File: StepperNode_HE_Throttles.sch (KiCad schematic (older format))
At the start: 2 parts

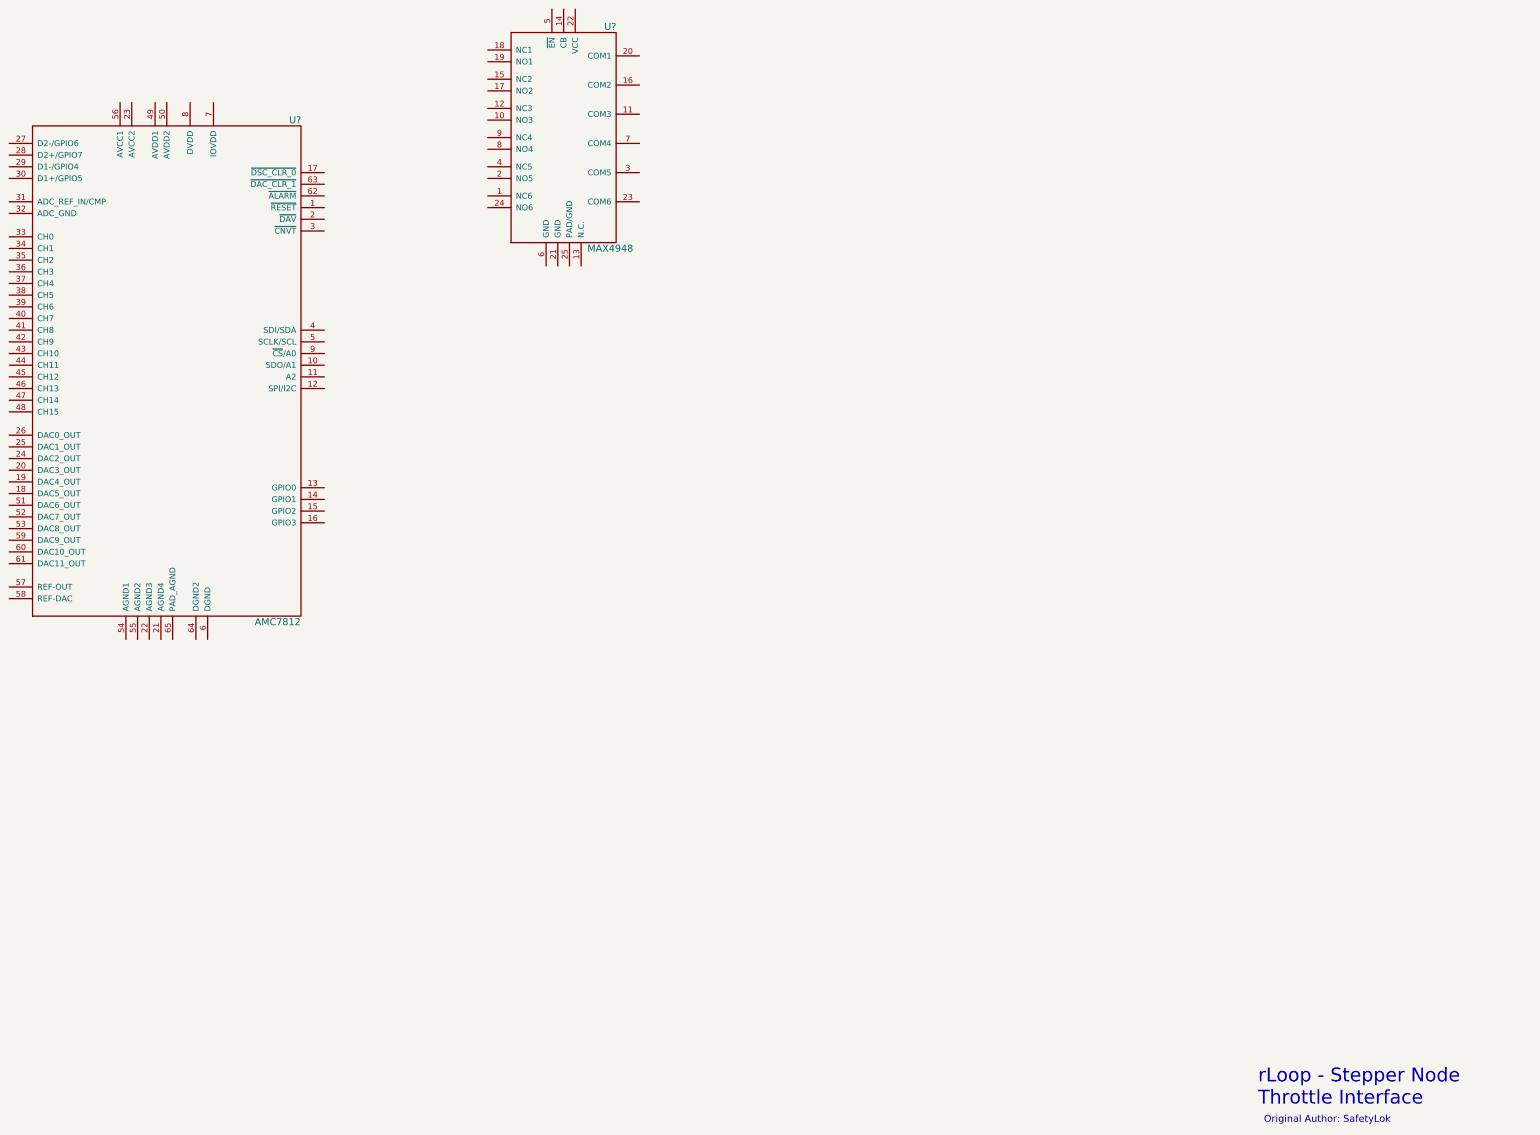
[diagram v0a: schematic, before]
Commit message: Commit after KiCad Crashed
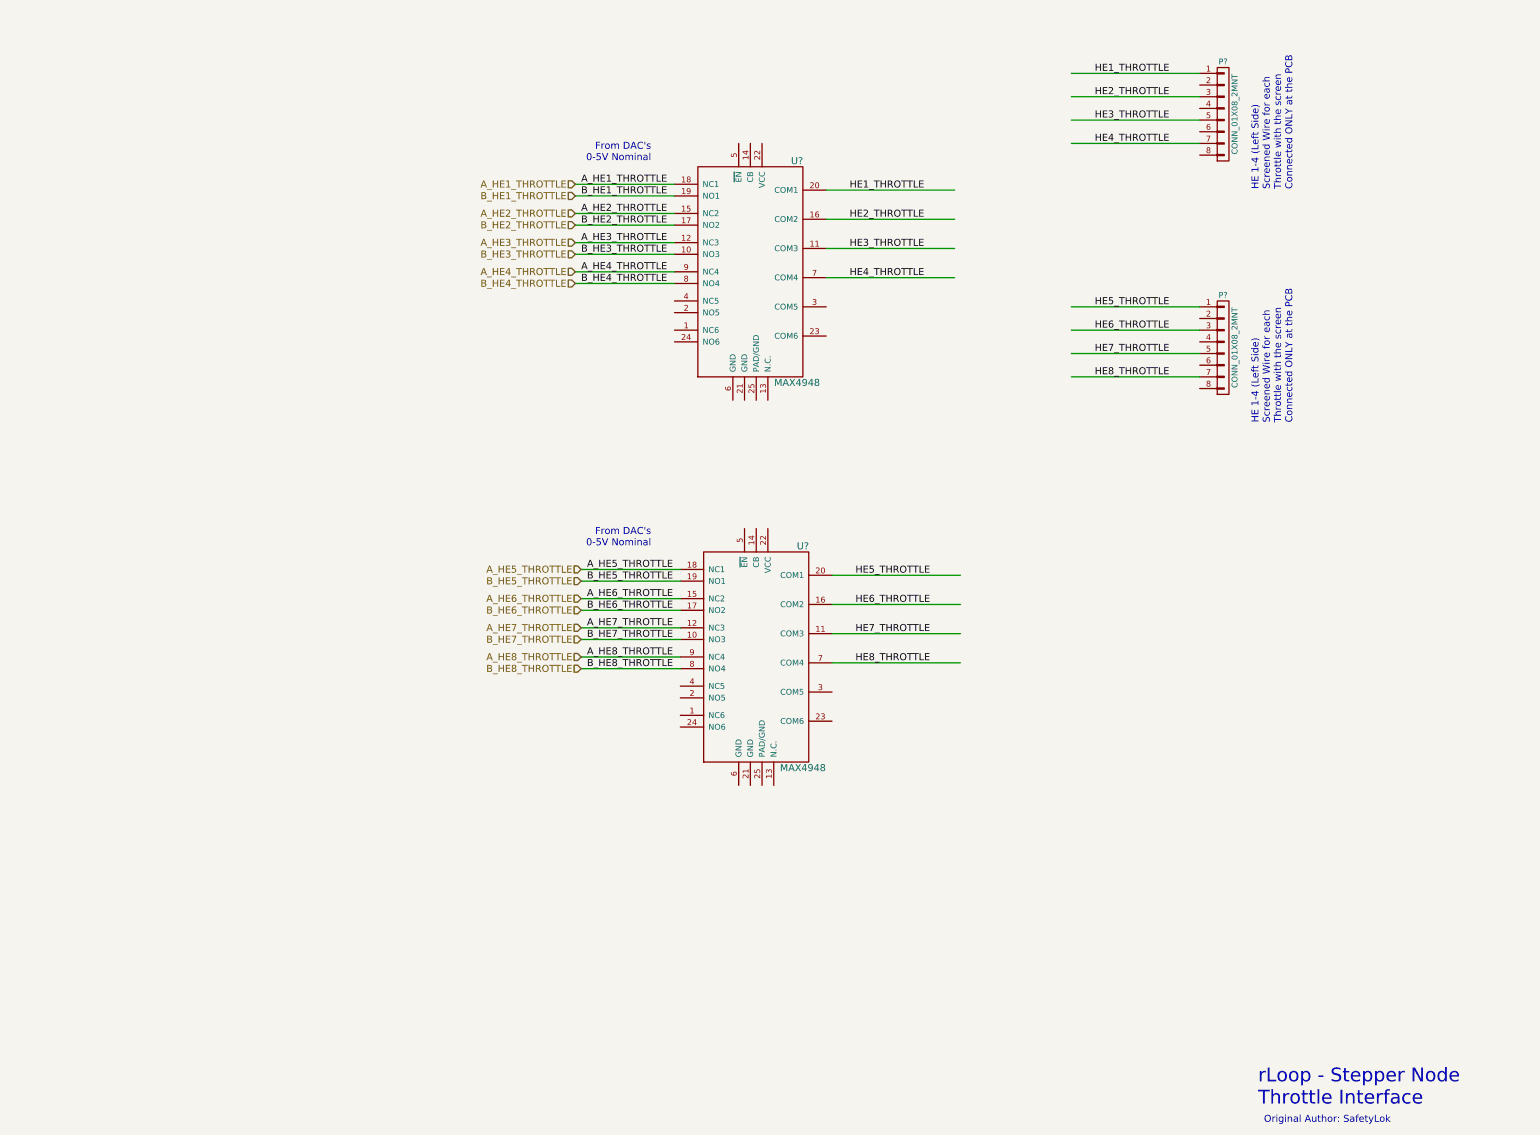
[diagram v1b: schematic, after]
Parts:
- removed U?: AMC7812, symbol AMC7812
- added P? (x2): CONN_01X08_2MNT, symbol CONN_01X08_2MNT
- added U?: MAX4948, symbol MAX4948
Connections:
- net labels added: A_HE1_THROTTLE, A_HE2_THROTTLE, A_HE3_THROTTLE, A_HE4_THROTTLE, A_HE5_THROTTLE, A_HE6_THROTTLE, A_HE7_THROTTLE, A_HE8_THROTTLE, B_HE1_THROTTLE, B_HE2_THROTTLE, B_HE3_THROTTLE, B_HE4_THROTTLE, B_HE5_THROTTLE, B_HE6_THROTTLE, B_HE7_THROTTLE, B_HE8_THROTTLE, HE1_THROTTLE, HE2_THROTTLE, HE3_THROTTLE, HE4_THROTTLE, HE5_THROTTLE, HE6_THROTTLE, HE7_THROTTLE, HE8_THROTTLE
- wire segments 0 -> 32
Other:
- note added: "From DAC's\n0-5V Nominal\n"
- note added: "HE 1-4 (Left Side)\nScreened Wire for each \nThrottle with the screen\nConnected ONLY at the PCB\n"
- moved on the sheet: U?
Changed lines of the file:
@@
 $Descr A3 16535 11693
 encoding utf-8
-Sheet 5 5
+Sheet 5 8
 Title "Throttle Interface"
 Date ""
@@
 L MAX4948 U?
 U 1 1 57503E43
-P 5500 2950
-F 0 "U?" H 6350 4800 60  0000 C CNN
-F 1 "MAX4948" H 6350 2900 60  0000 C CNN
-F 2 "" H 5500 3700 60  0000 C CNN
-F 3 "" H 5500 3700 60  0000 C CNN
-	1    5500 2950
-	1    0    0    -1
-$EndComp
-$Comp
-L AMC7812 U?
-U 1 1 57504099
-P 1400 6150
-F 0 "U?" H 3650 10400 60  0000 C CNN
-F 1 "AMC7812" H 3500 6100 60  0000 C CNN
-F 2 "" H 2700 8850 60  0000 C CNN
-F 3 "" H 2700 8850 60  0000 C CNN
-	1    1400 6150
-	1    0    0    -1
-$EndComp
+P 7100 4100
+F 0 "U?" H 7950 5950 60  0000 C CNN
+F 1 "MAX4948" H 7950 4050 60  0000 C CNN
+F 2 "" H 7100 4850 60  0000 C CNN
+F 3 "" H 7100 4850 60  0000 C CNN
+	1    7100 4100
+	1    0    0    -1
+$EndComp
+Wire Wire Line
+	6900 2450 6050 2450
+Wire Wire Line
+	6900 2550 6050 2550
+Text Label 6100 2450 0    60   ~ 0
+A_HE1_THROTTLE
+Text Label 6100 2550 0    60   ~ 0
+B_HE1_THROTTLE
+Wire Wire Line
+	8200 2500 9300 2500
+Text Label 8400 2500 0    60   ~ 0
+HE1_THROTTLE
+Wire Wire Line
+	6900 2700 6050 2700
+Wire Wire Line
+	6900 2800 6050 2800
+Text Label 6100 2700 0    60   ~ 0
+A_HE2_THROTTLE
+Text Label 6100 2800 0    60   ~ 0
+B_HE2_THROTTLE
+Wire Wire Line
+	6900 2950 6050 2950
+Wire Wire Line
+	6900 3050 6050 3050
+Text Label 6100 2950 0    60   ~ 0
+A_HE3_THROTTLE
+Text Label 6100 3050 0    60   ~ 0
+B_HE3_THROTTLE
+Wire Wire Line
+	6900 3200 6050 3200
+Wire Wire Line
+	6900 3300 6050 3300
+Text Label 6100 3200 0    60   ~ 0
+A_HE4_THROTTLE
+Text Label 6100 3300 0    60   ~ 0
+B_HE4_THROTTLE
+Text Notes 6700 2260 2    60   ~ 0
+From DAC's\n0-5V Nominal\n
+Wire Wire Line
+	8200 2750 9300 2750
+Text Label 8400 2750 0    60   ~ 0
+HE2_THROTTLE
+Wire Wire Line
+	8200 3000 9300 3000
+Text Label 8400 3000 0    60   ~ 0
+HE3_THROTTLE
+Wire Wire Line
+	8200 3250 9300 3250
+Text Label 8400 3250 0    60   ~ 0
+HE4_THROTTLE
+$Comp
+L MAX4948 U?
+U 1 1 57537B35
+P 7150 7400
+F 0 "U?" H 8000 9250 60  0000 C CNN
+F 1 "MAX4948" H 8000 7350 60  0000 C CNN
+F 2 "" H 7150 8150 60  0000 C CNN
+F 3 "" H 7150 8150 60  0000 C CNN
+	1    7150 7400
+	1    0    0    -1
+$EndComp
+Wire Wire Line
+	6950 5750 6100 5750
+Wire Wire Line
+	6950 5850 6100 5850
+Text Label 6150 5750 0    60   ~ 0
+A_HE5_THROTTLE
+Text Label 6150 5850 0    60   ~ 0
+B_HE5_THROTTLE
+Wire Wire Line
+	8250 5800 9350 5800
+Text Label 8450 5800 0    60   ~ 0
+HE5_THROTTLE
+Wire Wire Line
+	6950 6000 6100 6000
+Wire Wire Line
+	6950 6100 6100 6100
+Text Label 6150 6000 0    60   ~ 0
+A_HE6_THROTTLE
+Text Label 6150 6100 0    60   ~ 0
+B_HE6_THROTTLE
+Wire Wire Line
+	6950 6250 6100 6250
+Wire Wire Line
+	6950 6350 6100 6350
+Text Label 6150 6250 0    60   ~ 0
+A_HE7_THROTTLE
+Text Label 6150 6350 0    60   ~ 0
+B_HE7_THROTTLE
+Wire Wire Line
+	6950 6500 6100 6500
+Wire Wire Line
+	6950 6600 6100 6600
+Text Label 6150 6500 0    60   ~ 0
+A_HE8_THROTTLE
+Text Label 6150 6600 0    60   ~ 0
+B_HE8_THROTTLE
+Text Notes 6700 5560 2    60   ~ 0
+From DAC's\n0-5V Nominal\n
+Wire Wire Line
+	8250 6050 9350 6050
+Text Label 8450 6050 0    60   ~ 0
+HE6_THROTTLE
+Wire Wire Line
+	8250 6300 9350 6300
+Text Label 8450 6300 0    60   ~ 0
+HE7_THROTTLE
+Wire Wire Line
+	8250 6550 9350 6550
+Text Label 8450 6550 0    60   ~ 0
+HE8_THROTTLE
+$Comp
+L CONN_01X08_2MNT P?
+U 1 1 57537DBD
+P 11600 1850
+F 0 "P?" H 11600 2300 50  0000 C CNN
+F 1 "CONN_01X08_2MNT" V 11700 1850 50  0000 C CNN
+F 2 "" H 11600 1850 50  0000 C CNN
+F 3 "" H 11600 1850 50  0000 C CNN
+	1    11600 1850
+	1    0    0    -1
+$EndComp
+Wire Wire Line
+	10300 1500 11400 1500
+Text Label 10500 1500 0    60   ~ 0
+HE1_THROTTLE
+Wire Wire Line
+	10300 1700 11400 1700
+Text Label 10500 1700 0    60   ~ 0
+HE2_THROTTLE
+Wire Wire Line
+	10300 1900 11400 1900
+Text Label 10500 1900 0    60   ~ 0
+HE3_THROTTLE
+Wire Wire Line
+	10300 2100 11400 2100
+Text Label 10500 2100 0    60   ~ 0
+HE4_THROTTLE
+Text Notes 12200 2500 1    60   ~ 0
+HE 1-4 (Left Side)\nScreened Wire for each \nThrottle with the screen\nConnected ONLY at the PCB\n
+$Comp
+L CONN_01X08_2MNT P?
+U 1 1 57537EFF
+P 11600 3850
+F 0 "P?" H 11600 4300 50  0000 C CNN
+F 1 "CONN_01X08_2MNT" V 11700 3850 50  0000 C CNN
+F 2 "" H 11600 3850 50  0000 C CNN
+F 3 "" H 11600 3850 50  0000 C CNN
+	1    11600 3850
+	1    0    0    -1
+$EndComp
+Wire Wire Line
+	10300 3500 11400 3500
+Text Label 10500 3500 0    60   ~ 0
+HE5_THROTTLE
+Wire Wire Line
+	10300 3700 11400 3700
+Text Label 10500 3700 0    60   ~ 0
+HE6_THROTTLE
+Wire Wire Line
+	10300 3900 11400 3900
+Text Label 10500 3900 0    60   ~ 0
+HE7_THROTTLE
+Wire Wire Line
+	10300 4100 11400 4100
+Text Label 10500 4100 0    60   ~ 0
+HE8_THROTTLE
+Text Notes 12200 4500 1    60   ~ 0
+HE 1-4 (Left Side)\nScreened Wire for each \nThrottle with the screen\nConnected ONLY at the PCB\n
+Text HLabel 6050 2450 0    60   Input ~ 0
+A_HE1_THROTTLE
+Text HLabel 6050 2700 0    60   Input ~ 0
+A_HE2_THROTTLE
+Text HLabel 6050 2950 0    60   Input ~ 0
+A_HE3_THROTTLE
+Text HLabel 6050 3200 0    60   Input ~ 0
+A_HE4_THROTTLE
+Text HLabel 6100 5750 0    60   Input ~ 0
+A_HE5_THROTTLE
+Text HLabel 6100 6000 0    60   Input ~ 0
+A_HE6_THROTTLE
+Text HLabel 6100 6250 0    60   Input ~ 0
+A_HE7_THROTTLE
+Text HLabel 6100 6500 0    60   Input ~ 0
+A_HE8_THROTTLE
+Text HLabel 6050 2550 0    60   Input ~ 0
+B_HE1_THROTTLE
+Text HLabel 6050 2800 0    60   Input ~ 0
+B_HE2_THROTTLE
+Text HLabel 6050 3050 0    60   Input ~ 0
+B_HE3_THROTTLE
+Text HLabel 6050 3300 0    60   Input ~ 0
+B_HE4_THROTTLE
+Text HLabel 6100 5850 0    60   Input ~ 0
+B_HE5_THROTTLE
+Text HLabel 6100 6100 0    60   Input ~ 0
+B_HE6_THROTTLE
+Text HLabel 6100 6350 0    60   Input ~ 0
+B_HE7_THROTTLE
+Text HLabel 6100 6600 0    60   Input ~ 0
+B_HE8_THROTTLE
 $EndSCHEMATC
